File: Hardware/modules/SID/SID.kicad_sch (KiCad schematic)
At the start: 14 parts, among them J1 Bus_PCI_6502, J2 POT_X, J3 POT_Y, J4 POT_X, U1 74HC138, U2 8580

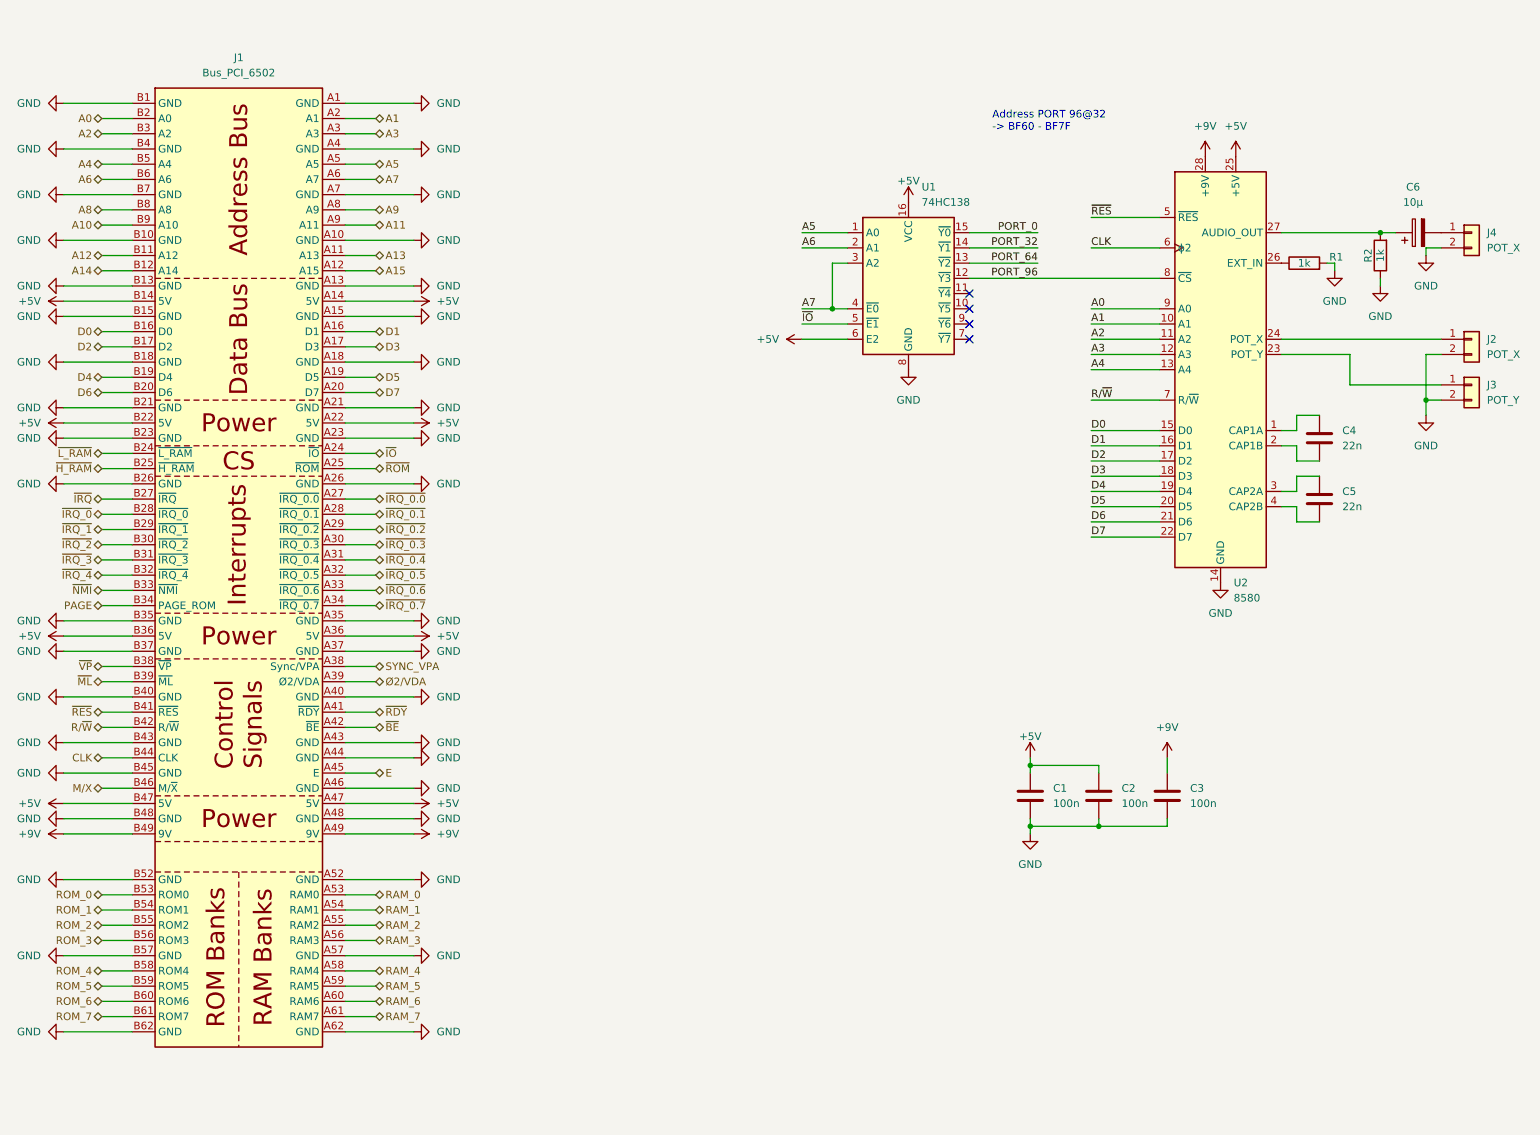
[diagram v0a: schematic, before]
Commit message: Hardware Update Add MyCPU VGA Module Beautify all Schematics minor Error corrections Readme Update
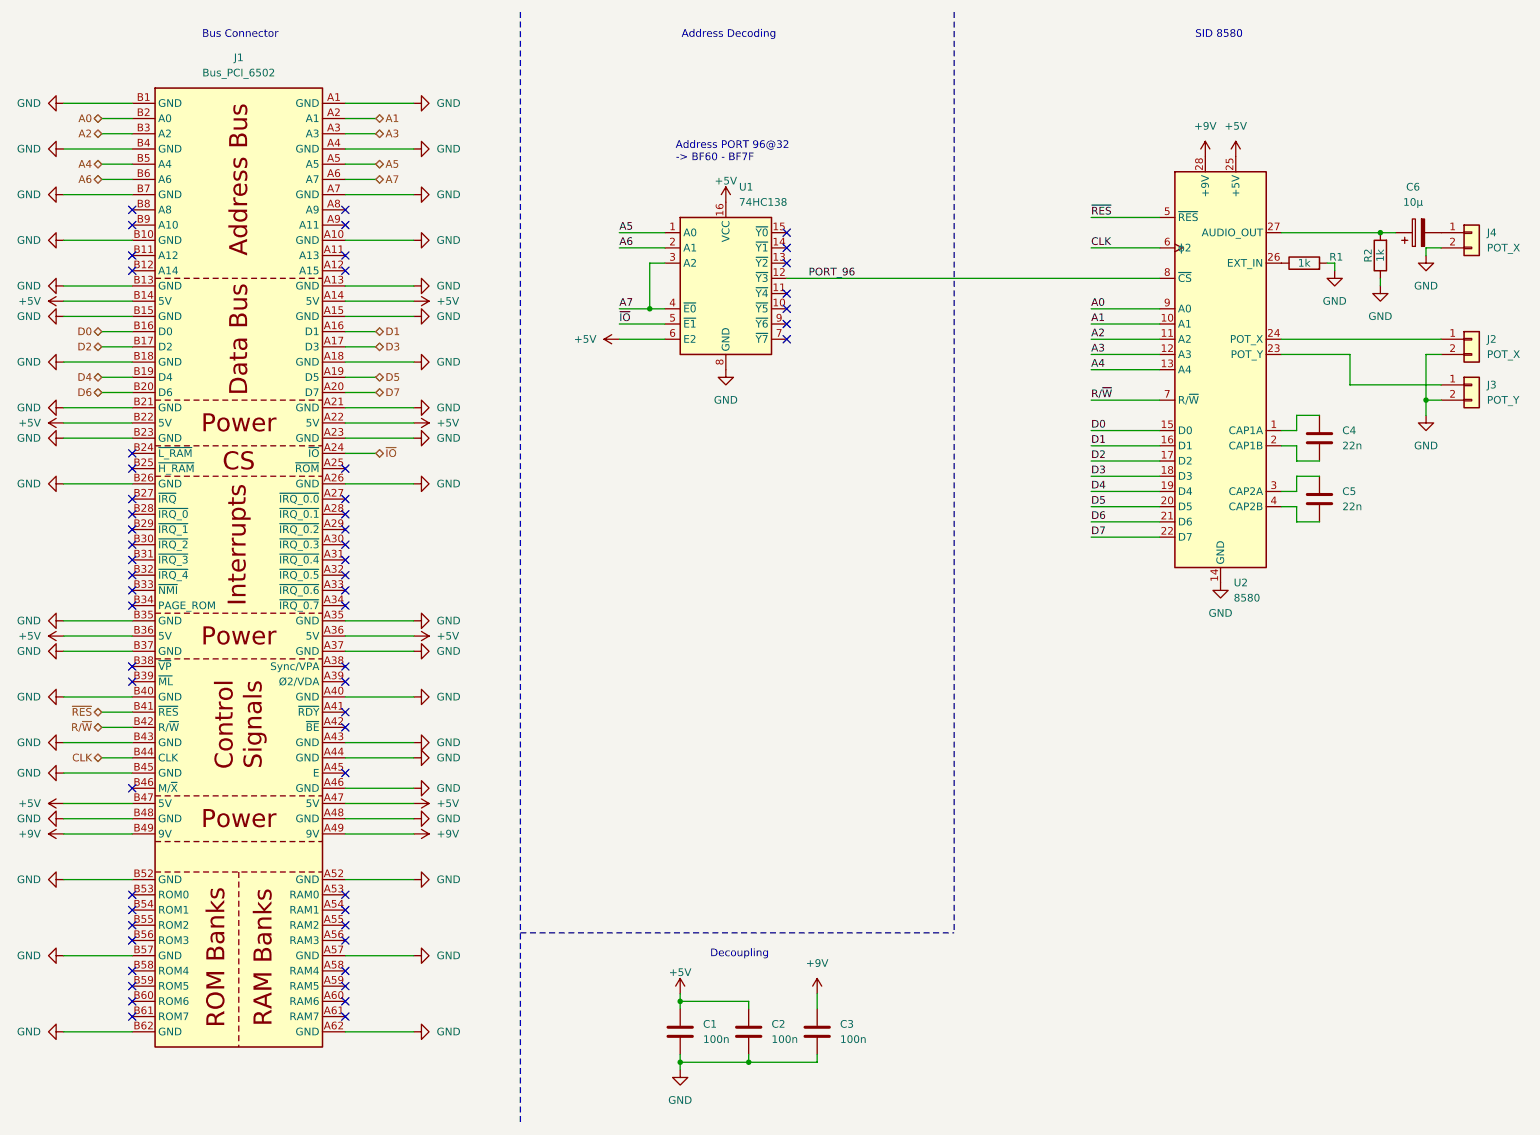
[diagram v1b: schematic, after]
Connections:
- net A10: no longer names the net of J1.B9 (A10)
- net A11: no longer names the net of J1.A9 (A11)
- net A12: no longer names the net of J1.B11 (A12)
- net A13: no longer names the net of J1.A11 (A13)
- net A14: no longer names the net of J1.B12 (A14)
- net A15: no longer names the net of J1.A12 (A15)
- net A8: no longer names the net of J1.B8 (A8)
- net A9: no longer names the net of J1.A8 (A9)
- net E: no longer names the net of J1.A45 (E)
- net M/X: no longer names the net of J1.B46 (M/~{X})
- net PAGE: no longer names the net of J1.B34 (PAGE_ROM)
- net PORT_0: no longer names the net of U1.15 (~{Y0})
- net PORT_32: no longer names the net of U1.14 (~{Y1})
- net PORT_64: no longer names the net of U1.13 (~{Y2})
- net RAM_0: no longer names the net of J1.A53 (RAM0)
- net RAM_1: no longer names the net of J1.A54 (RAM1)
- net RAM_2: no longer names the net of J1.A55 (RAM2)
- net RAM_3: no longer names the net of J1.A56 (RAM3)
- net RAM_4: no longer names the net of J1.A58 (RAM4)
- net RAM_5: no longer names the net of J1.A59 (RAM5)
- net RAM_6: no longer names the net of J1.A60 (RAM6)
- net RAM_7: no longer names the net of J1.A61 (RAM7)
- net ROM_0: no longer names the net of J1.B53 (ROM0)
- net ROM_1: no longer names the net of J1.B54 (ROM1)
- net ROM_2: no longer names the net of J1.B55 (ROM2)
- net ROM_3: no longer names the net of J1.B56 (ROM3)
- net ROM_4: no longer names the net of J1.B58 (ROM4)
- net ROM_5: no longer names the net of J1.B59 (ROM5)
- net ROM_6: no longer names the net of J1.B60 (ROM6)
- net ROM_7: no longer names the net of J1.B61 (ROM7)
- net SYNC_VPA: no longer names the net of J1.A38 (Sync/VPA)
- net ~{BE}: no longer names the net of J1.A42 (~{BE})
- net ~{H_RAM}: no longer names the net of J1.B25 (~{H_RAM})
- net ~{IRQ_0.0}: no longer names the net of J1.A27 (~{IRQ_0.0})
- net ~{IRQ_0.1}: no longer names the net of J1.A28 (~{IRQ_0.1})
- net ~{IRQ_0.2}: no longer names the net of J1.A29 (~{IRQ_0.2})
- net ~{IRQ_0.3}: no longer names the net of J1.A30 (~{IRQ_0.3})
- net ~{IRQ_0.4}: no longer names the net of J1.A31 (~{IRQ_0.4})
- net ~{IRQ_0.5}: no longer names the net of J1.A32 (~{IRQ_0.5})
- net ~{IRQ_0.6}: no longer names the net of J1.A33 (~{IRQ_0.6})
- net ~{IRQ_0.7}: no longer names the net of J1.A34 (~{IRQ_0.7})
- net ~{IRQ_0}: no longer names the net of J1.B28 (~{IRQ_0})
- net ~{IRQ_1}: no longer names the net of J1.B29 (~{IRQ_1})
- net ~{IRQ_2}: no longer names the net of J1.B30 (~{IRQ_2})
- net ~{IRQ_3}: no longer names the net of J1.B31 (~{IRQ_3})
- net ~{IRQ_4}: no longer names the net of J1.B32 (~{IRQ_4})
- net ~{IRQ}: no longer names the net of J1.B27 (~{IRQ})
- net ~{L_RAM}: no longer names the net of J1.B24 (~{L_RAM})
- net ~{ML}: no longer names the net of J1.B39 (~{ML})
- net ~{NMI}: no longer names the net of J1.B33 (~{NMI})
- net ~{RDY}: no longer names the net of J1.A41 (~{RDY})
- net ~{ROM}: no longer names the net of J1.A25 (~{ROM})
- net ~{VP}: no longer names the net of J1.B38 (~{VP})
- net Ø2/VDA: no longer names the net of J1.A39 (Ø2/VDA)
- no-connect marks 4 -> 58
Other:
- note added: "Address Decoding"
- note added: "Bus Connector"
- note added: "Decoupling"
- note added: "SID 8580"
- company: (none) -> Synthron
- title: (none) -> S65xx Computer System
- moved on the sheet: C1, C2, C3, U1

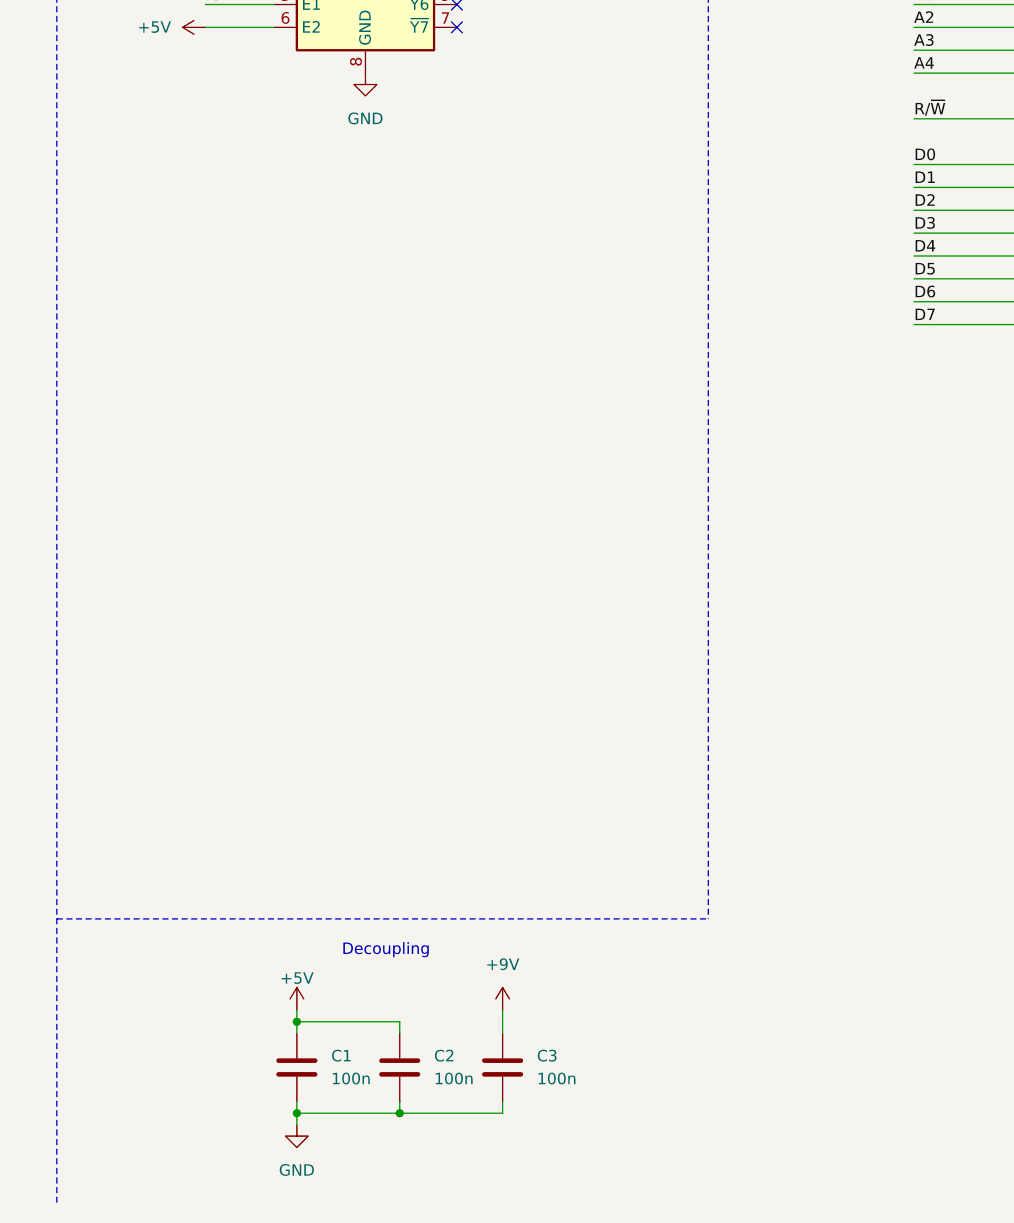
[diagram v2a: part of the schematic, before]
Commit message: Hardware Review Pt. 1 fix Address Decoding for Strobe Generators add bulk capacitance to every board fix wiring of Prototyping Board
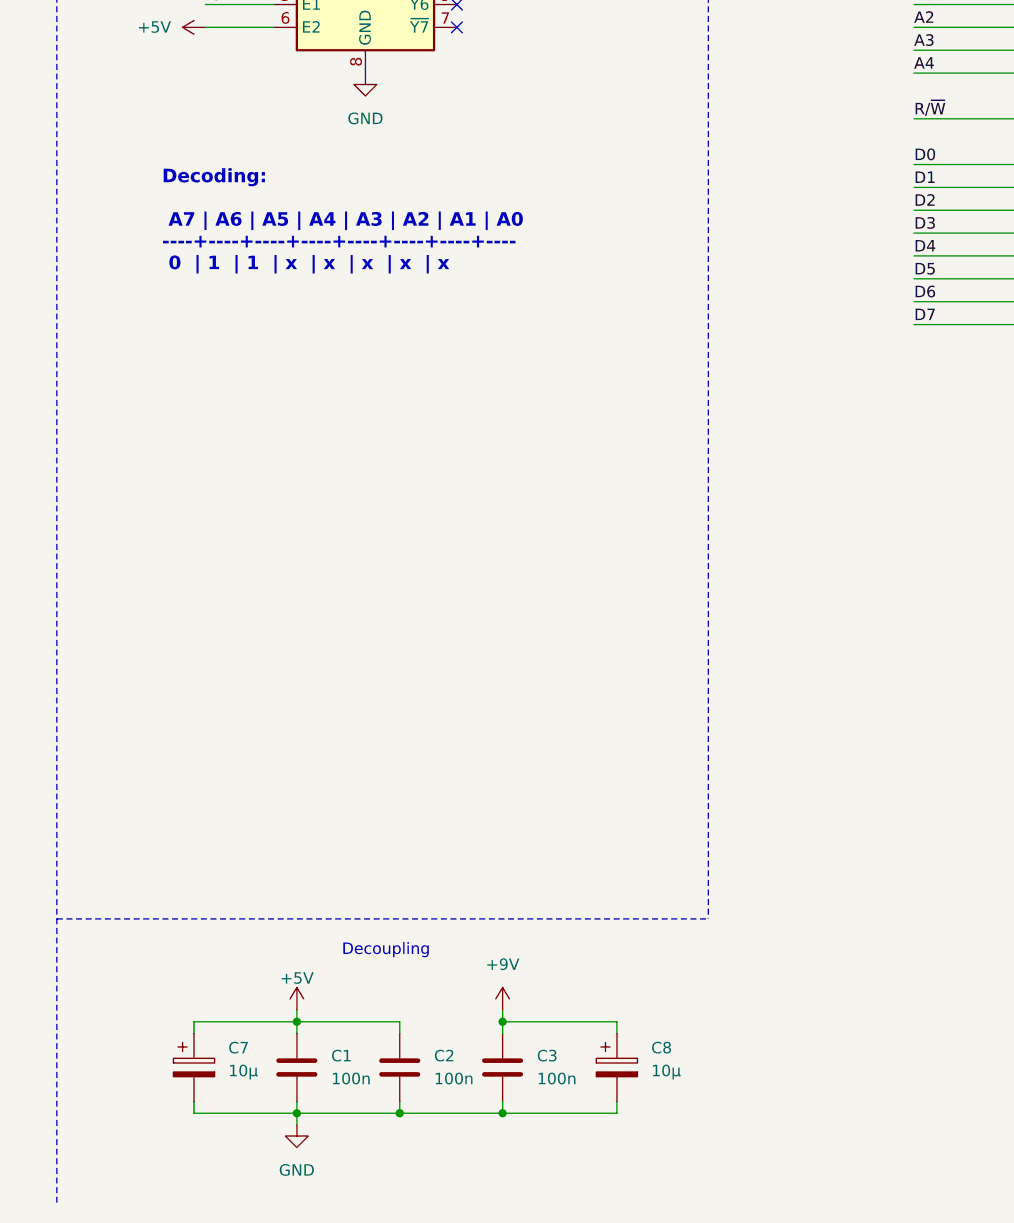
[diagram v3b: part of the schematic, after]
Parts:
- added C7, C8: 10µ, Capacitor_THT:CP_Radial_D5.0mm_P2.50mm, symbol Device:C_Polarized
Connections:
- net +5V: now also C7.1
- net +9V: now also C8.1
- net GND: now also C7.2, C8.2
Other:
- note added: "Decoding: A7 | A6 | A5 | A4 | A3 | A2 | A1 | A0 ----+----+----+----+----+----+----+---- 0 | 1 | 1 | x | x | x | x | x"
